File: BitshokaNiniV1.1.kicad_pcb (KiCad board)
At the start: 4 copper layers, 56.5 x 99.8 mm, 172 parts, among them J1 54-00164, J2 TC2030-IDC, J3 Conn_01x04, J4 Conn_01x06, J5 USB_C_Receptacle_USB2.0, J6 Conn_01x04, J7 Conn_01x04, Q1 MMBT3906, Q3 MMBT3906, Q4 MMBT2222A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

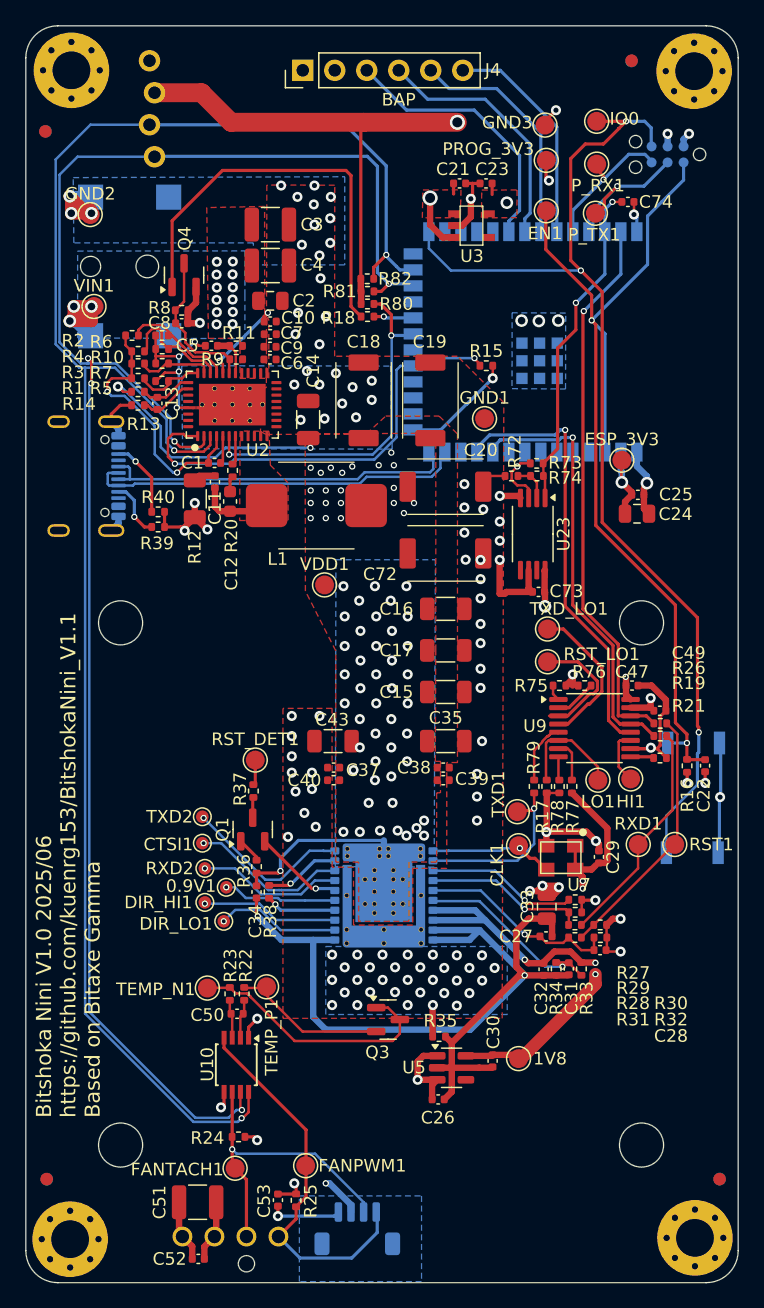
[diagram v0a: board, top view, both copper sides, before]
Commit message: New Inductor & BOM fix
Changed the inductor and cleaned up files for JLCPCB order.
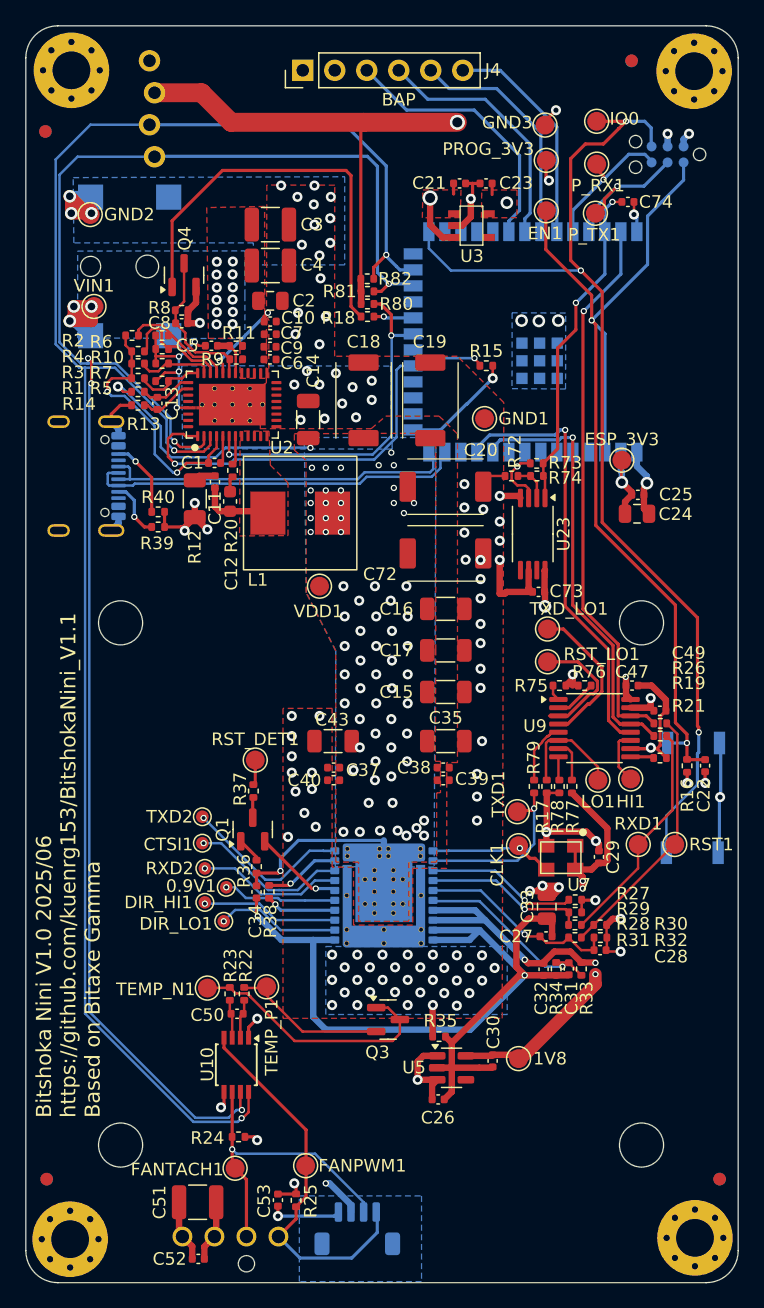
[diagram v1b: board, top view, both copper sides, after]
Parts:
- L1: value 75nH -> 72nH; footprint bitaxe:SLC1049 -> bitaxe:FP0805R1
- moved L1 1.42 mm to (99.0, 86.2), turned to 0 degrees
- moved VDD1 0.41 mm to (100.5, 92.0)
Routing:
- net /VDD: vias 72 -> 73
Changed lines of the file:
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@@
 		(tags "test point SMD pad")
 		(property "Reference" "GND2"
-			(at 0 -1.648 0)
+			(at 3.1 0 0)
 			(layer "F.SilkS")
 			(effects
@@
 		(tags "resistor")
 		(property "Reference" "R29"
-			(at -4.60341 -6.01159 0)
+			(at -4.60341 0.28841 0)
 			(layer "F.SilkS")
 			(effects
@@
 		(tags "resistor")
 		(property "Reference" "R31"
-			(at -4.61 -6.51159 0)
+			(at -4.61 -0.21159 0)
 			(layer "F.SilkS")
 			(effects
@@
 		(tags "resistor")
 		(property "Reference" "R30"
-			(at -5.62341 -6.21159 0)
+			(at -5.62341 0.08841 0)
 			(layer "F.SilkS")
 			(effects
@@
 		(tags "capacitor")
 		(property "Reference" "C23"
-			(at -0.48 1.13 180)
+			(at -2.38 0.03 180)
 			(layer "F.SilkS")
 			(effects
@@
 		(tags "resistor")
 		(property "Reference" "R27"
-			(at -4.60341 -5.81159 0)
+			(at -4.60341 0.48841 0)
 			(layer "F.SilkS")
 			(effects
@@
 		(tags "capacitor")
 		(property "Reference" "C28"
-			(at -5.63341 -6.81159 0)
+			(at -5.63341 -0.51159 0)
 			(layer "F.SilkS")
 			(effects
@@
 		(tags "resistor")
 		(property "Reference" "R28"
-			(at -4.61 -6.21159 0)
+			(at -4.61 0.08841 0)
 			(layer "F.SilkS")
 			(effects
@@
 		(tags "test point SMD pad")
 		(property "Reference" "GND1"
-			(at 0 -1.648 0)
+			(at 3.1 0 0)
 			(layer "F.SilkS")
 			(effects
@@
 		)
 	)
-	(footprint "bitaxe:SLC1049"
+	(footprint "bitaxe:FP0805R1"
 		(layer "F.Cu")
-		(at 100.25 85.6 180)
+		(at 98.965 86.2)
 		(property "Reference" "L1"
-			(at 3.07 -4.245 0)
+			(at -3.365 5.3 0)
 			(unlocked yes)
 			(layer "F.SilkS")
@@
 			)
 		)
-		(property "Value" "75nH"
-			(at 0 1 180)
+		(property "Value" "72nH"
+			(at 0 1 0)
 			(unlocked yes)
 			(layer "F.Fab")
+			(hide yes)
 			(effects
 				(font
@@
 		)
 		(property "Datasheet" "https://www.coilcraft.com/getmedia/ef564b79-aee7-4fb3-aabd-a8bf1c568496/slc1049.pdf"
-			(at 0 0 180)
+			(at 0 0 0)
 			(unlocked yes)
 			(layer "F.Fab")
@@
 		)
 		(property "Description" "Inductor"
-			(at 0 0 180)
+			(at 0 0 0)
 			(unlocked yes)
 			(layer "F.Fab")
@@
 		)
 		(property "PARTNO" "SLC1049-750MLB"
-			(at 0 0 180)
+			(at 0 0 0)
 			(unlocked yes)
 			(layer "F.Fab")
@@
 		)
 		(property "DK" ""
-			(at 0 0 180)
+			(at 0 0 0)
 			(unlocked yes)
 			(layer "F.Fab")
@@
 		)
 		(property "Mouser" ""
-			(at 0 0 180)
+			(at 0 0 0)
 			(unlocked yes)
 			(layer "F.Fab")
@@
 		)
 		(property "HEIGHT" ""
-			(at 0 0 180)
+			(at 0 0 0)
 			(unlocked yes)
 			(layer "F.Fab")
@@
 		(sheetfile "power.kicad_sch")
 		(attr smd)
-		(fp_line
-			(start -3 3.44)
-			(end 3 3.44)
-			(stroke
-				(width 0.1)
-				(type default)
-			)
-			(layer "F.SilkS")
-		)
-		(fp_line
-			(start -3 -3.44)
-			(end 3 -3.44)
-			(stroke
-				(width 0.1)
-				(type default)
-			)
-			(layer "F.SilkS")
-		)
 		(fp_rect
-			(start -5.6 -3.94)
-			(end 5.6 3.94)
+			(start -4.5 -4.5)
+			(end 4.5 4.5)
 			(stroke
-				(width 0.1)
-				(type default)
+				(width 0.12)
+				(type solid)
 			)
 			(fill no)
-			(layer "F.CrtYd")
+			(layer "F.SilkS")
 		)
 		(fp_text user "${REFERENCE}"
-			(at 0 2.5 180)
+			(at -3.039436 4.386339 0)
 			(unlocked yes)
 			(layer "F.Fab")
@@
 			)
 		)
-		(pad "1" smd roundrect
-			(at 3.95 0 180)
-			(size 3.3 3.43)
+		(pad "1" smd rect
+			(at -2.565 0)
+			(size 2.79 3.43)
 			(layers "F.Cu" "F.Mask" "F.Paste")
-			(roundrect_rratio 0.15)
 			(net 9 "/Power/SW")
 			(pinfunction "1")
 			(pintype "passive")
-			(thermal_bridge_angle 45)
 		)
-		(pad "2" smd roundrect
-			(at -3.95 0 180)
-			(size 3.3 3.43)
+		(pad "2" smd rect
+			(at 2.565 0)
+			(size 2.79 3.43)
 			(layers "F.Cu" "F.Mask" "F.Paste")
-			(roundrect_rratio 0.15)
 			(net 2 "/VDD")
 			(pinfunction "2")
 			(pintype "passive")
-			(thermal_bridge_angle 45)
 		)
 		(embedded_fonts no)
@@
 		(tags "resistor")
 		(property "Reference" "R32"
-			(at 5.60341 6.51159 0)
+			(at 5.60341 0.21159 0)
 			(layer "F.SilkS")
 			(effects
@@
 		(tags "VQFN NoLead")
 		(property "Reference" "U2"
-			(at -3.61 2.02 180)
+			(at -3.41 3.92 180)
 			(layer "F.SilkS")
 			(effects
@@
 	(footprint "TestPoint:TestPoint_Pad_D1.5mm"
 		(layer "F.Cu")
-		(at 100.9 91.9)
+		(at 100.5 92)
 		(descr "SMD pad as test Point, diameter 1.5mm")
 		(tags "test point SMD pad")
 		(property "Reference" "VDD1"
-			(at 0 -1.648 0)
+			(at -0.1 2 0)
 			(layer "F.SilkS")
 			(effects
@@
 		(tags "capacitor")
 		(property "Reference" "C21"
-			(at -0.52 -1.13 0)
+			(at -2.42 -0.03 0)
 			(layer "F.SilkS")
 			(effects
@@
 		(tags "esp32-s3")
 		(property "Reference" "U4"
-			(at 8.71 -10.53 270)
+			(at 10.71 -9.83 0)
 			(layer "B.SilkS")
 			(effects
@@
 		(tags "tag connect programming header pogo pins")
 		(property "Reference" "J2"
-			(at -0.17 -2.37 0)
+			(at -0.07 -2.77 0)
 			(layer "B.SilkS")
 			(effects
@@
 	)
 	(via
-		(at 100.6 83)
-		(size 0.5)
-		(drill 0.3)
-		(layers "F.Cu" "B.Cu")
-		(net 2)
-	)
-	(via
 		(at 107.5 99)
 		(size 0.8)
@@
 	)
 	(via
-		(at 103.1 82.5)
+		(at 99.9 82.6)
 		(size 0.5)
 		(drill 0.3)
@@
 	)
 	(via
-		(at 101.4 82.6)
+		(at 101 82.6)
 		(size 0.5)
 		(drill 0.3)
@@
 	)
 	(via
-		(at 99.8 82.6)
-		(size 0.5)
-		(drill 0.3)
-		(layers "F.Cu" "B.Cu")
-		(net 2)
-	)
-	(via
 		(at 101 85.4)
 		(size 0.5)
@@
 	)
 	(via
+		(at 99.8 87.7)
+		(size 0.5)
+		(drill 0.3)
+		(layers "F.Cu" "B.Cu")
+		(net 2)
+	)
+	(via
 		(at 105 101.3)
 		(size 0.8)
@@
 	)
 	(via
+		(at 99.8 84.4)
+		(size 0.5)
+		(drill 0.3)
+		(layers "F.Cu" "B.Cu")
+		(net 2)
+	)
+	(via
 		(at 106.4 85.4)
 		(size 0.5)
@@
 	)
 	(via
+		(at 102.2 87.7)
+		(size 0.5)
+		(drill 0.3)
+		(layers "F.Cu" "B.Cu")
+		(net 2)
+	)
+	(via
 		(at 107.4 92)
 		(size 0.8)
@@
 	)
 	(via
-		(at 99.8 84.4)
-		(size 0.5)
-		(drill 0.3)
-		(layers "F.Cu" "B.Cu")
-		(net 2)
-	)
-	(via
 		(at 116.19941 82.49941)
 		(size 0.5)
@@
 	)
 	(via
-		(at 102.3 83)
+		(at 102.2 82.6)
 		(size 0.5)
 		(drill 0.3)
@@
 	)
 	(via
+		(at 101 87.7)
+		(size 0.5)
+		(drill 0.3)
+		(layers "F.Cu" "B.Cu")
+		(net 2)
+	)
+	(via
 		(at 102.5 94.4)
 		(size 0.8)
@@
 		(polygon
 			(pts
-				(xy 96.6 82.4) (xy 96.49 79.7) (xy 94.2 79.69) (xy 94.16 86.79) (xy 98 86.763549) (xy 98 83.8)
+				(xy 96.6 82.4) (xy 96.49 79.7) (xy 94.2 79.69) (xy 94.153111 88.012785) (xy 98 87.986286) (xy 98 83.8)
 			)
 		)
@@
 		(polygon
 			(pts
-				(xy 95.82 79.73) (xy 96.29 79.96) (xy 104.22511 79.906384) (xy 105.757585 78.5) (xy 109.994526 78.5)
-				(xy 111.452 79.918647) (xy 111.452 106) (xy 110.6 106) (xy 110.6 114.4) (xy 107.9 114.4) (xy 107.9 118.9)
-				(xy 103.2 118.9) (xy 103.2 114.3) (xy 101.5 114.3) (xy 101.5 101.7) (xy 97.6 101.7) (xy 97.6 126.3)
-				(xy 115 126.3) (xy 115.128186 77.428186) (xy 111.45 73.75) (xy 101.7 73.75) (xy 101.71 60.17) (xy 96.32 60.16)
-				(xy 96.28 76.22) (xy 95.82 76.44)
+				(xy 95.8 79.5) (xy 104.6 79.5) (xy 105.757585 78.5) (xy 109.994526 78.5) (xy 111.452 79.918647)
+				(xy 111.452 106) (xy 110.6 106) (xy 110.6 114.4) (xy 107.9 114.4) (xy 107.9 118.9) (xy 103.2 118.9)
+				(xy 103.2 114.3) (xy 101.5 114.3) (xy 101.5 101.7) (xy 97.6 101.7) (xy 97.6 126.3) (xy 115 126.3)
+				(xy 115.128186 77.428186) (xy 111.45 73.75) (xy 101.7 73.75) (xy 101.71 60.17) (xy 96.32 60.16)
+				(xy 96.280835 75.884819) (xy 95.822195 76.104169)
 			)
 		)
@@
 				(xy 109.728 97.028) (xy 109.689617 105.9) (xy 110.1 105.9) (xy 110.1 108.4) (xy 109.8 108.4) (xy 109.8 113.9)
 				(xy 107.6 113.9) (xy 107.6 118.6) (xy 103.6 118.6) (xy 103.6 113.9) (xy 101.8 113.9) (xy 101.79 97.13)
-				(xy 99.38 92.39) (xy 99.360783 79.918) (xy 109.728 79.858038)
+				(xy 99.447691 92.523134) (xy 99.431476 81.99952) (xy 98.5 81.2) (xy 98.5 79.9) (xy 109.728 79.858038)
 			)
 		)
@@
 		(polygon
 			(pts
-				(xy 109.6 114.3) (xy 101.75 114.25) (xy 101.803369 89.9) (xy 109.7 89.9)
+				(xy 109.6 114.3) (xy 101.75 114.25) (xy 101.79 97.13) (xy 99.447691 92.523134) (xy 99.288364 80.2)
+				(xy 109.739755 80.2)
 			)
 		)
